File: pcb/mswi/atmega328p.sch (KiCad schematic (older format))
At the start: 86 parts, among them J401 USART, Y401 16MHz

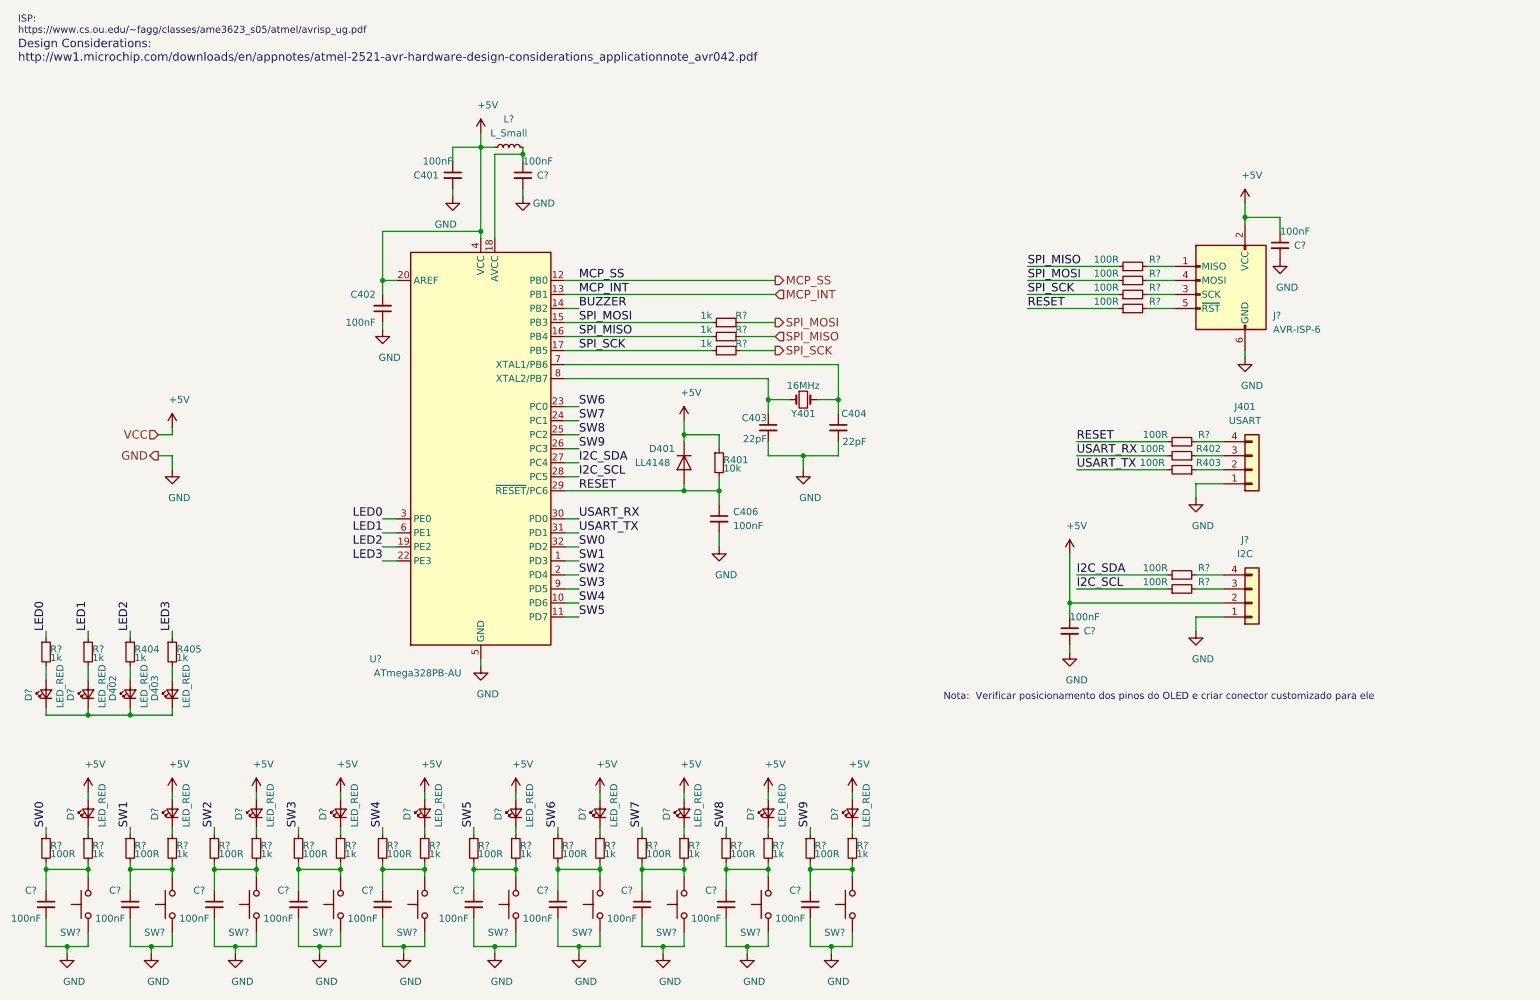
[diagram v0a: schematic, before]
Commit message: switches reworked, buzzer added
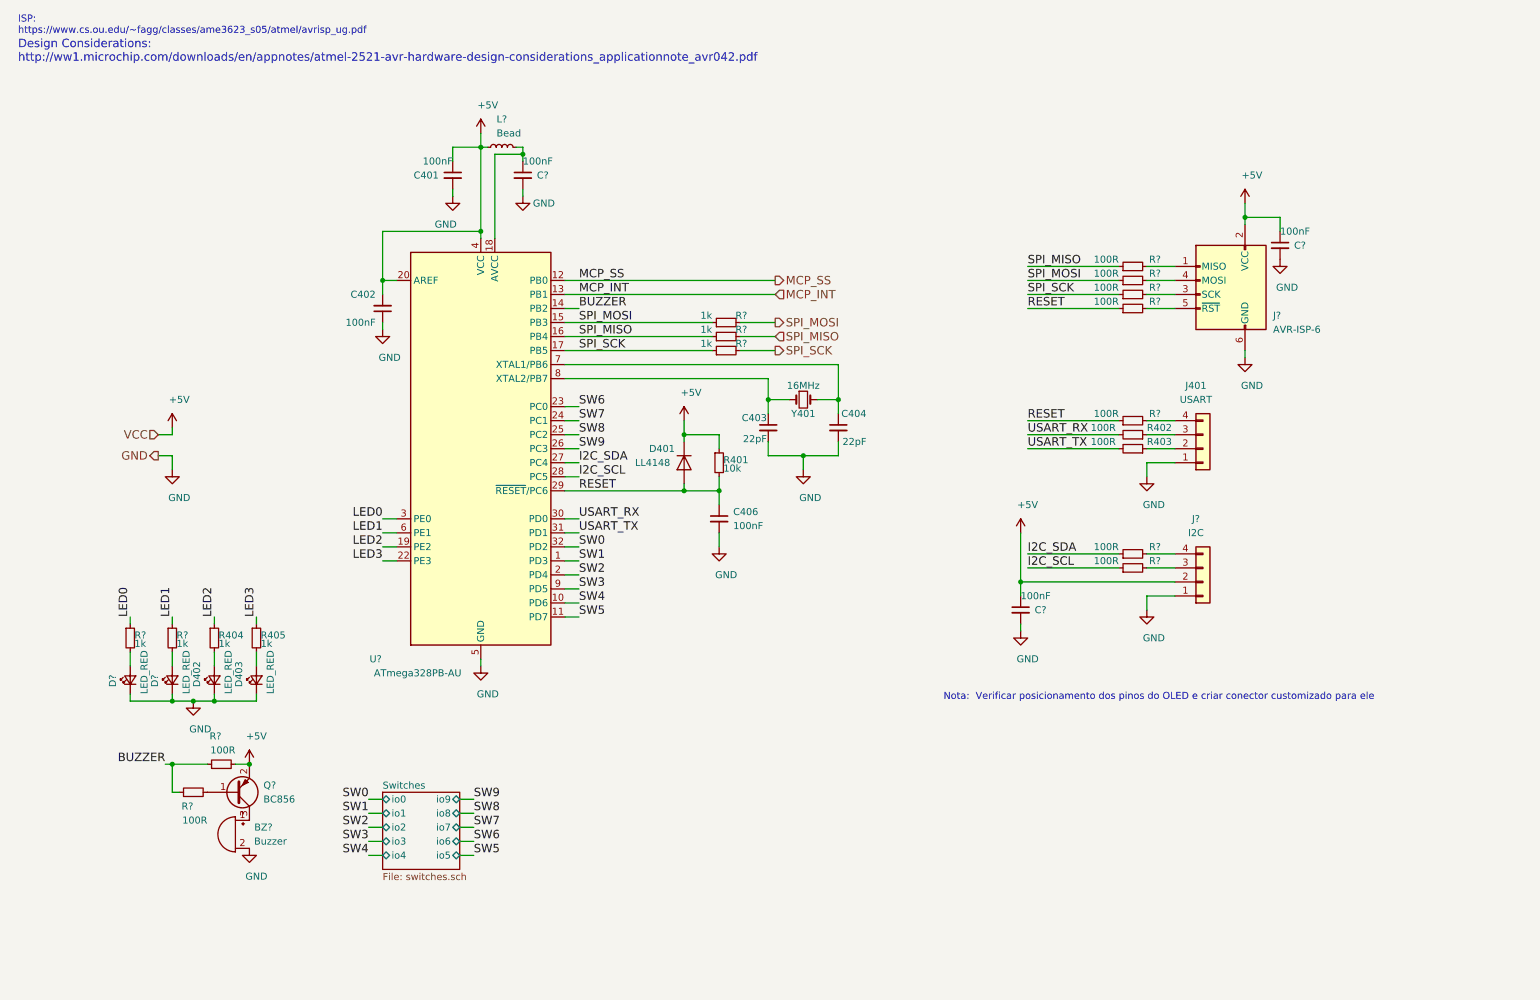
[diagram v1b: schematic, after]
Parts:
- removed C? (x10): 100nF, Capacitor_SMD:C_0805_2012Metric_Pad1.15x1.40mm_HandSolder, symbol Device:C_Small
- removed D? (x10): LED_RED, LED_SMD:LED_0805_2012Metric_Pad1.15x1.40mm_HandSolder, symbol Device:LED_Small
- removed R? (x10): 1k, Resistor_SMD:R_0805_2012Metric_Pad1.15x1.40mm_HandSolder, symbol Device:R_Small
- removed R? (x10): 100R, Resistor_SMD:R_0805_2012Metric_Pad1.15x1.40mm_HandSolder, symbol Device:R_Small
- removed SW? (x10): SW_Push, symbol Switch:SW_Push
- added BZ?: Buzzer, symbol Device:Buzzer
- added Q?: BC856, Package_TO_SOT_SMD:SOT-23, symbol Transistor_BJT:BC856
- added R? (x2): 100R, Resistor_SMD:R_0805_2012Metric_Pad1.15x1.40mm_HandSolder, symbol Device:R_Small
- L?: value L_Small -> Bead
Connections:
- net +5V: now also Q?.2 (E), R?.2
- net BUZZER: now also R?.1, R?.1
- net GND: now also D402.1 (K), D403.1 (K), D?.1 (K), D?.1 (K), BZ?.2 (+)
- new net: Q?.1 (B), R?.2
- new net: BZ?.1 (-), Q?.3 (C)
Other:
- moved on the sheet: C?, D402, D403, D?, J401, J?, L?, R402, R403, R404, R405, R?

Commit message: Schematics Annotated
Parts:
- gave numbers to parts that had none: 25
- renumbered C401 to C301, C402 to C304, C403 to C305, C404 to C306, C406 to C307, D401 to D301, D402 to D304, D403 to D305, J401 to J302, R402 to R309, R403 to R310, R401 to R311, R404 to R316, R405 to R317, Y401 to Y301
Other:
- moved on the sheet: BZ301, Q301, R318, R319

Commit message: Footprints associated
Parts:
- added TP?: BUZZ_out, TestPoint:TestPoint_Pad_2.0x2.0mm, symbol Connector:TestPoint
- added TP?: BUZZ_in, TestPoint:TestPoint_Pad_2.0x2.0mm, symbol Connector:TestPoint
- added TP?: SDA, TestPoint:TestPoint_Pad_2.0x2.0mm, symbol Connector:TestPoint
- added TP?: SCL, TestPoint:TestPoint_Pad_2.0x2.0mm, symbol Connector:TestPoint
- added TP?: RST, TestPoint:TestPoint_Pad_2.0x2.0mm, symbol Connector:TestPoint
- added TP?: RX, TestPoint:TestPoint_Pad_2.0x2.0mm, symbol Connector:TestPoint
- added TP?: TX, TestPoint:TestPoint_Pad_2.0x2.0mm, symbol Connector:TestPoint
- J301: footprint (none) -> Connector_IDC:IDC-Header_2x03_P2.54mm_Horizontal
- L301: footprint (none) -> Inductor_SMD:L_0805_2012Metric_Pad1.15x1.40mm_HandSolder
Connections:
- net BUZZER: now also TP?.1
- net I2C_SCL: now also TP?.1
- net I2C_SDA: now also TP?.1
- net RESET: now also TP?.1
- net USART_RX: now also TP?.1
- net USART_TX: now also TP?.1
- net at BZ301.1 (-), Q301.3 (C): now also TP?.1
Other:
- moved on the sheet: BZ301, R318

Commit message: Test points added. Buzz footprint added
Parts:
- BZ301: footprint (none) -> Buzzer_Beeper:Buzzer_12x9.5RM7.6
- gave numbers to parts that had none: 7
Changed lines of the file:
@@
 F 0 "BZ301" H 1950 6700 50  0000 C CNN
 F 1 "Buzzer" H 1900 6600 50  0000 C CNN
-F 2 "" V 2125 6750 50  0001 C CNN
+F 2 "Buzzer_Beeper:Buzzer_12x9.5RM7.6" V 2125 6750 50  0001 C CNN
 F 3 "~" V 2125 6750 50  0001 C CNN
 	1    2150 6650
@@
 P 2400 6500
 AR Path="/5AABFC1B/5DB6352B" Ref="TP?"  Part="1"
-AR Path="/5AACA401/5DB6352B" Ref="TP?"  Part="1"
-F 0 "TP?" V 2350 6750 50  0000 C CNN
+AR Path="/5AACA401/5DB6352B" Ref="TP307"  Part="1"
+F 0 "TP307" V 2350 6750 50  0000 C CNN
 F 1 "BUZZ_out" V 2450 6850 50  0000 C CNN
 F 2 "TestPoint:TestPoint_Pad_2.0x2.0mm" H 2600 6500 50  0001 C CNN
@@
 P 1700 6250
 AR Path="/5AABFC1B/5DB75F53" Ref="TP?"  Part="1"
-AR Path="/5AACA401/5DB75F53" Ref="TP?"  Part="1"
-F 0 "TP?" V 1600 6500 50  0000 C CNN
+AR Path="/5AACA401/5DB75F53" Ref="TP306"  Part="1"
+F 0 "TP306" V 1600 6500 50  0000 C CNN
 F 1 "BUZZ_in" V 1700 6600 50  0000 C CNN
 F 2 "TestPoint:TestPoint_Pad_2.0x2.0mm" H 1900 6250 50  0001 C CNN
@@
 P 8200 4300
 AR Path="/5AABFC1B/5DB80116" Ref="TP?"  Part="1"
-AR Path="/5AACA401/5DB80116" Ref="TP?"  Part="1"
-F 0 "TP?" H 8300 4500 50  0000 C CNN
+AR Path="/5AACA401/5DB80116" Ref="TP304"  Part="1"
+F 0 "TP304" H 8300 4500 50  0000 C CNN
 F 1 "SDA" H 8300 4400 50  0000 C CNN
 F 2 "TestPoint:TestPoint_Pad_2.0x2.0mm" H 8400 4300 50  0001 C CNN
@@
 P 8150 4350
 AR Path="/5AABFC1B/5DB8FE76" Ref="TP?"  Part="1"
-AR Path="/5AACA401/5DB8FE76" Ref="TP?"  Part="1"
-F 0 "TP?" H 8050 4550 50  0000 C CNN
+AR Path="/5AACA401/5DB8FE76" Ref="TP305"  Part="1"
+F 0 "TP305" H 8050 4550 50  0000 C CNN
 F 1 "SCL" H 8050 4500 50  0000 C CNN
 F 2 "TestPoint:TestPoint_Pad_2.0x2.0mm" H 8350 4350 50  0001 C CNN
@@
 P 8050 3350
 AR Path="/5AABFC1B/5DB9E1B1" Ref="TP?"  Part="1"
-AR Path="/5AACA401/5DB9E1B1" Ref="TP?"  Part="1"
-F 0 "TP?" H 7950 3550 50  0000 C CNN
+AR Path="/5AACA401/5DB9E1B1" Ref="TP303"  Part="1"
+F 0 "TP303" H 7950 3550 50  0000 C CNN
 F 1 "RST" H 7950 3500 50  0000 C CNN
 F 2 "TestPoint:TestPoint_Pad_2.0x2.0mm" H 8250 3350 50  0001 C CNN
@@
 P 8150 3200
 AR Path="/5AABFC1B/5DB9E6A4" Ref="TP?"  Part="1"
-AR Path="/5AACA401/5DB9E6A4" Ref="TP?"  Part="1"
-F 0 "TP?" H 8050 3400 50  0000 C CNN
+AR Path="/5AACA401/5DB9E6A4" Ref="TP302"  Part="1"
+F 0 "TP302" H 8050 3400 50  0000 C CNN
 F 1 "RX" H 8050 3350 50  0000 C CNN
 F 2 "TestPoint:TestPoint_Pad_2.0x2.0mm" H 8350 3200 50  0001 C CNN
@@
 P 8250 3050
 AR Path="/5AABFC1B/5DB9E9B2" Ref="TP?"  Part="1"
-AR Path="/5AACA401/5DB9E9B2" Ref="TP?"  Part="1"
-F 0 "TP?" H 8150 3250 50  0000 C CNN
+AR Path="/5AACA401/5DB9E9B2" Ref="TP301"  Part="1"
+F 0 "TP301" H 8150 3250 50  0000 C CNN
 F 1 "TX" H 8150 3200 50  0000 C CNN
 F 2 "TestPoint:TestPoint_Pad_2.0x2.0mm" H 8450 3050 50  0001 C CNN

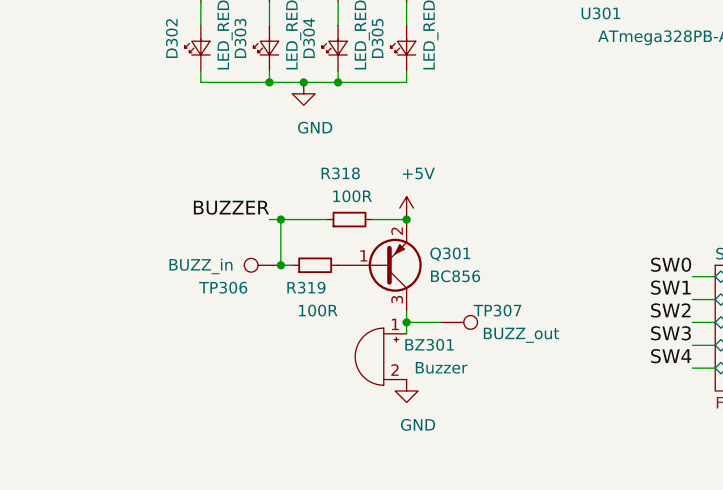
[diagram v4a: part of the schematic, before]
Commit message: ISP connector changed to vertical
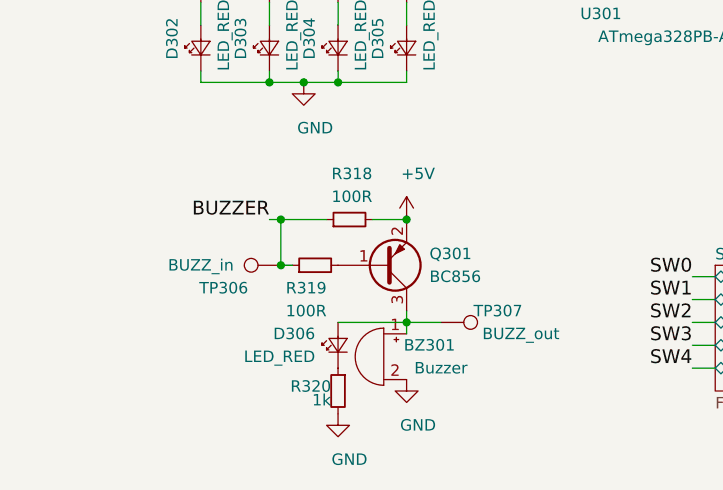
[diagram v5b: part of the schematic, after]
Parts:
- added D306: LED_RED, LED_SMD:LED_0805_2012Metric_Pad1.15x1.40mm_HandSolder, symbol Device:LED_Small
- added R320: 1k, Resistor_SMD:R_0805_2012Metric_Pad1.15x1.40mm_HandSolder, symbol Device:R_Small
- J301: footprint Connector_IDC:IDC-Header_2x03_P2.54mm_Horizontal -> Connector_IDC:IDC-Header_2x03_P2.54mm_Vertical
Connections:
- net GND: now also R320.2
- net at BZ301.1 (-), Q301.3 (C), TP307.1: now also D306.2 (A)
- new net: D306.1 (K), R320.1
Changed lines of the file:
@@
 EESchema Schematic File Version 4
-LIBS:main-cache
+LIBS:mswi-cache
 EELAYER 30 0
 EELAYER END
@@
 F 0 "J301" H 8900 2400 50  0000 R CNN
 F 1 "AVR-ISP-6" H 8900 2300 50  0000 R CNN
-F 2 "Connector_IDC:IDC-Header_2x03_P2.54mm_Horizontal" V 8950 2600 50  0001 C CNN
+F 2 "Connector_IDC:IDC-Header_2x03_P2.54mm_Vertical" V 8950 2600 50  0001 C CNN
 F 3 " ~" H 7925 2000 50  0001 C CNN
 	1    9200 2550
@@
 P 1850 6250
 F 0 "R319" V 1750 6200 50  0000 L CNN
-F 1 "100R" V 1650 6150 50  0000 L CNN
+F 1 "100R" V 1650 6200 50  0000 L CNN
 F 2 "Resistor_SMD:R_0805_2012Metric_Pad1.15x1.40mm_HandSolder" H 1850 6250 50  0001 C CNN
 F 3 "" H 1850 6250 50  0001 C CNN
@@
 U 1 1 5DA9E27C
 P 2000 6050
-F 0 "R318" V 2200 6000 50  0000 L CNN
+F 0 "R318" V 2200 5950 50  0000 L CNN
 F 1 "100R" V 2100 5950 50  0000 L CNN
 F 2 "Resistor_SMD:R_0805_2012Metric_Pad1.15x1.40mm_HandSolder" H 2000 6050 50  0001 C CNN
@@
 Wire Wire Line
 	8250 3650 8400 3650
+$Comp
+L Device:LED_Small D306
+U 1 1 5DAAE348
+P 1950 6600
+F 0 "D306" V 2000 6700 50  0000 L CNN
+F 1 "LED_RED" V 1900 6700 50  0000 L CNN
+F 2 "LED_SMD:LED_0805_2012Metric_Pad1.15x1.40mm_HandSolder" V 1950 6600 50  0001 C CNN
+F 3 "" V 1950 6600 50  0001 C CNN
+	1    1950 6600
+	0    -1   -1   0
+$EndComp
+$Comp
+L Device:R_Small R320
+U 1 1 5DAAE352
+P 1950 6800
+F 0 "R320" H 1980 6820 50  0000 L CNN
+F 1 "1k" H 1980 6760 50  0000 L CNN
+F 2 "Resistor_SMD:R_0805_2012Metric_Pad1.15x1.40mm_HandSolder" H 1950 6800 50  0001 C CNN
+F 3 "" H 1950 6800 50  0001 C CNN
+	1    1950 6800
+	-1   0    0    -1
+$EndComp
+Wire Wire Line
+	1950 6500 2250 6500
+$Comp
+L power:GND #PWR0321
+U 1 1 5DAC59DC
+P 1950 6900
+F 0 "#PWR0321" H 1950 6650 50  0001 C CNN
+F 1 "GND" H 2000 6700 50  0000 C CNN
+F 2 "" H 1950 6900 50  0001 C CNN
+F 3 "" H 1950 6900 50  0001 C CNN
+	1    1950 6900
+	1    0    0    -1
+$EndComp
 $EndSCHEMATC
